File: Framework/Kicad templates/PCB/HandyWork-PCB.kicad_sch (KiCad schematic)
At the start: 52 parts, among them J1 Conn_01x04, J2 Conn_02x04_Odd_Even, SW1 KXT3, SW2 KXT3, U1 RP2040, U2 W25Q16JV, U3 IS31FL3733B-QF, Y1 12.000 MHz

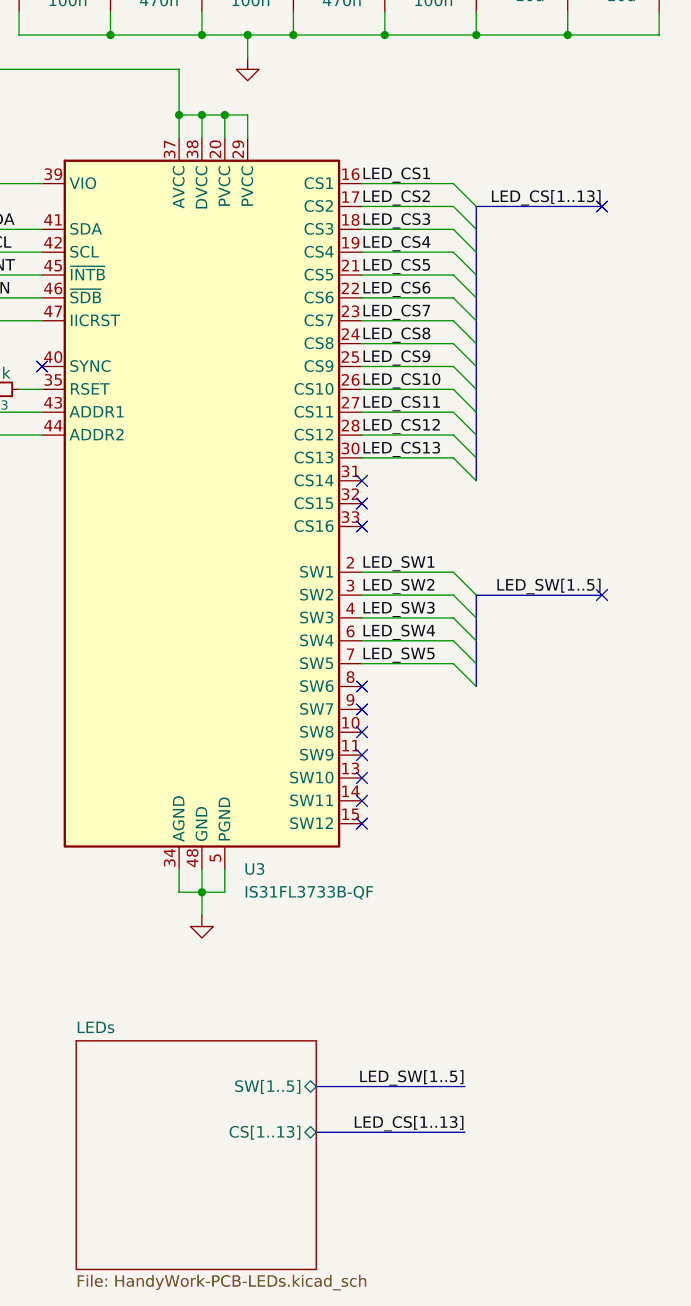
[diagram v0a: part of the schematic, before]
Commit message: HandyWork: Updating KiCad PCB template. Now complete.
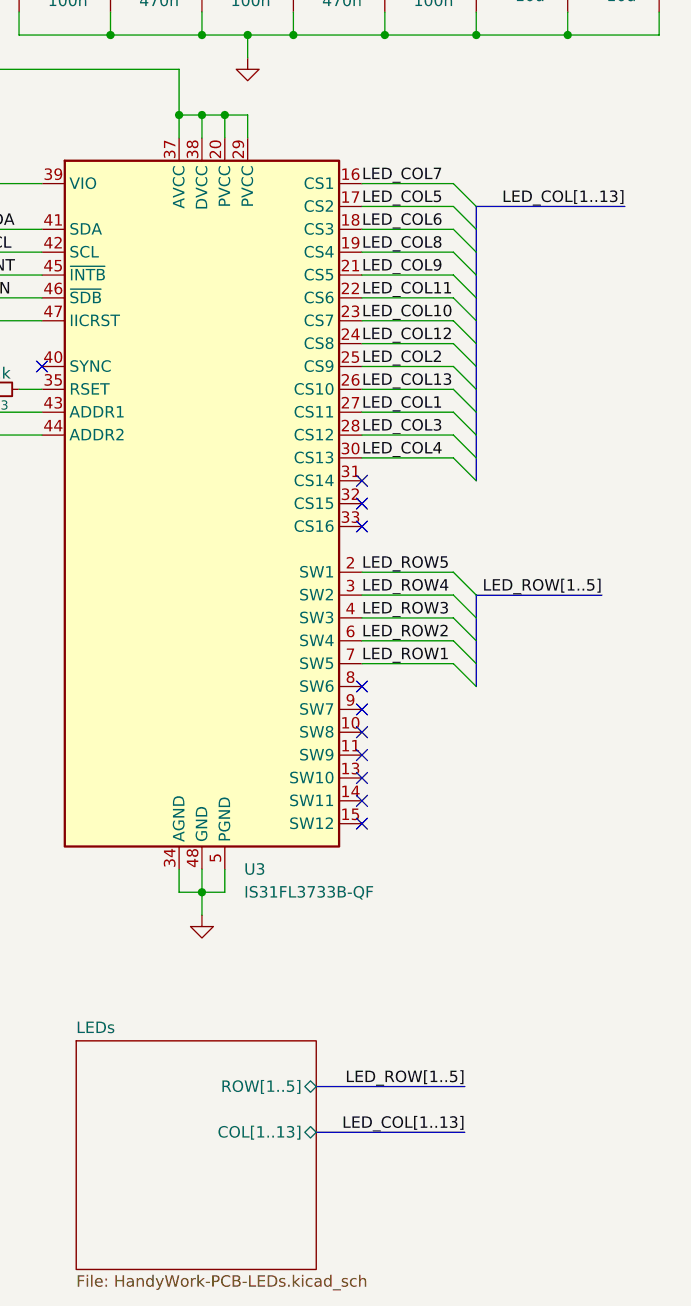
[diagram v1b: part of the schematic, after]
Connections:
- net LED_CS1 renamed LED_COL7
- net LED_CS10 renamed LED_COL13
- net LED_CS11 renamed LED_COL1
- net LED_CS12 renamed LED_COL3
- net LED_CS13 renamed LED_COL4
- net LED_CS2 renamed LED_COL5
- net LED_CS3 renamed LED_COL6
- net LED_CS4 renamed LED_COL8
- net LED_CS5 renamed LED_COL9
- net LED_CS6 renamed LED_COL11
- net LED_CS7 renamed LED_COL10
- net LED_CS8 renamed LED_COL12
- net LED_CS9 renamed LED_COL2
- net LED_SW1 renamed LED_ROW5
- net LED_SW2 renamed LED_ROW4
- net LED_SW3 renamed LED_ROW3
- net LED_SW4 renamed LED_ROW2
- net LED_SW5 renamed LED_ROW1
- no-connect marks 22 -> 20
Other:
- sheet LEDs ports: added COL[1..13], ROW[1..5]; removed CS[1..13], SW[1..5]
- title: (none) -> HandyWork - PCB Template

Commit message: HandyWork: Harmonise a few things, and add bind points with alu plates
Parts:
- added TP1, TP2, TP3, TP4, TP5, TP6: TestPoint, TestPoint:TestPoint_THTPad_2.5x2.5mm_Drill1.2mm, symbol Connector:TestPoint
- J1: now not fitted
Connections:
- net GND: now also TP1.1, TP2.1, TP3.1, TP4.1, TP5.1, TP6.1
